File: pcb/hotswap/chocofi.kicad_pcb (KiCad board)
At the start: 2 copper layers, 111.3 x 90 mm, 61 parts, among them J2 Conn_01x05, J3 Conn_01x02_Female, SW1 SW_SPDT, SW10 SW_PUSH, SW11 SW_PUSH, SW12 SW_PUSH, SW14 SW_PUSH, SW15 SW_PUSH, SW16 SW_PUSH, SW17 SW_PUSH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

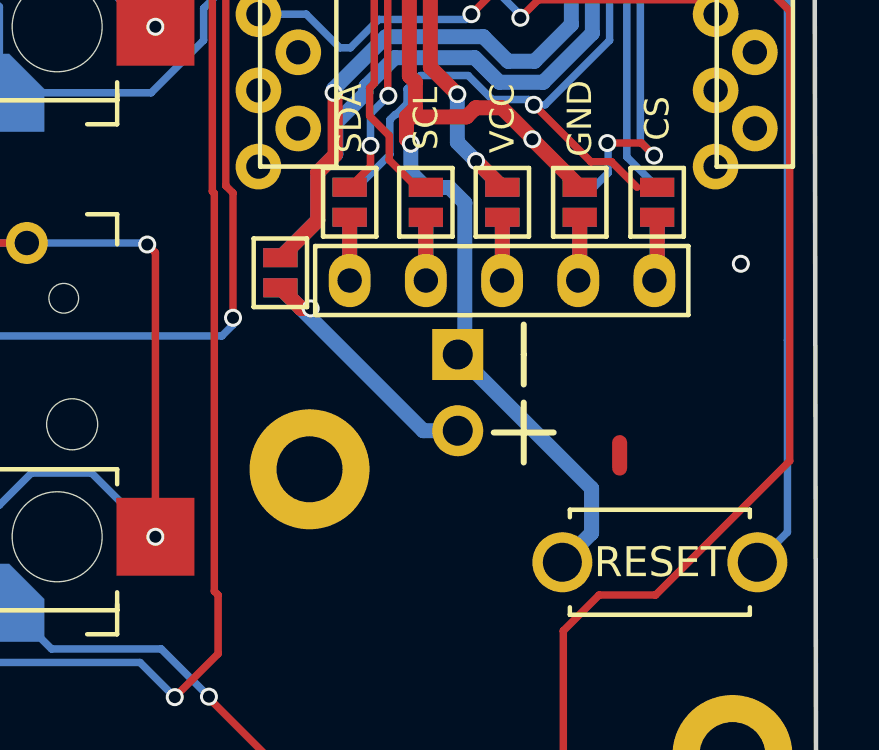
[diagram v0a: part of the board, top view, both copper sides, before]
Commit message: move reset button
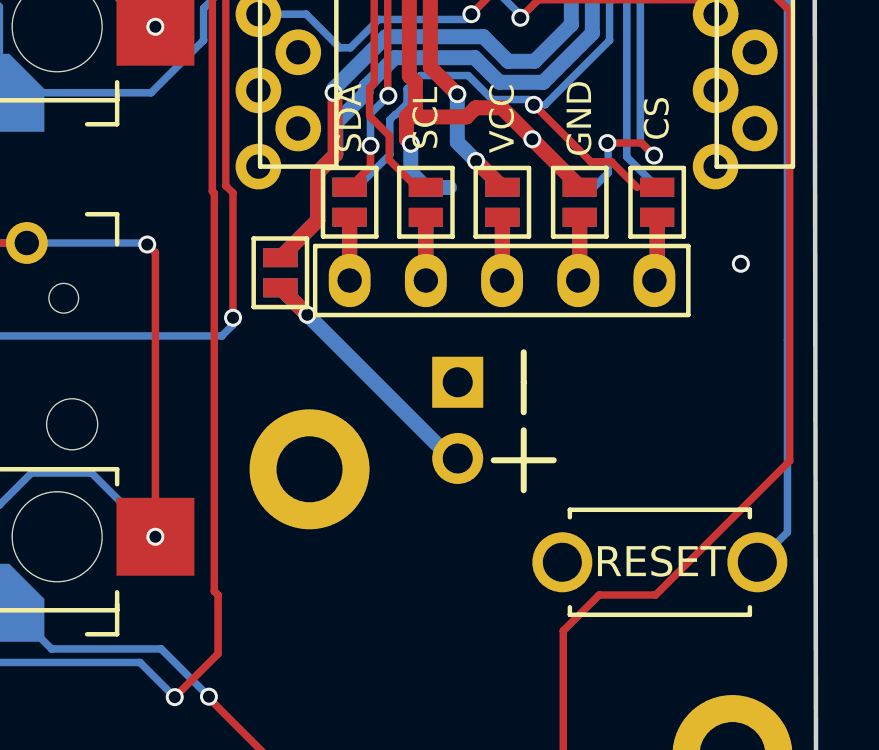
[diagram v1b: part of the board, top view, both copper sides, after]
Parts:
- moved J3 0.92 mm to (176.3, 94.0)
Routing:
- net GND: track 79.1 -> 63.2 mm
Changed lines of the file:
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@@
 		)
 		(pad_to_mask_clearance 0.2)
-		(solder_mask_min_width 0.1)
 		(allow_soldermask_bridges_in_footprints no)
 		(aux_axis_origin 145.73 12.66)
@@
 		(fp_arc
 			(start -1 3.7)
-			(mid -2.060661 3.260661)
+			(mid -2.060662 3.260662)
 			(end -2.5 2.2)
 			(stroke
@@
 		(fp_arc
 			(start -1 3.7)
-			(mid -2.060661 3.260661)
+			(mid -2.060662 3.260662)
 			(end -2.5 2.2)
 			(stroke
@@
 		)
 		(fp_line
-			(start 7 4.999999)
+			(start 7 4.999998)
 			(end 9.5 5)
 			(stroke
@@
 	(footprint "kbd:Battery_TH"
 		(layer "F.Cu")
-		(at 176.2625 93.075)
+		(at 176.2625 94)
 		(descr "Through hole straight pin header, 1x02, 2.54mm pitch, single row")
 		(tags "Through hole pin header THT 1x02 2.54mm single row")
 		(property "Reference" "J3"
-			(at 0 -2.33 360)
+			(at 0 -2.33 0)
 			(layer "Dwgs.User")
 			(effects
@@
 		)
 		(property "Value" "Conn_01x02_Female"
-			(at 0 4.87 360)
+			(at 0 4.87 0)
 			(layer "F.Fab")
 			(effects
@@
 		)
 		(property "Footprint" ""
-			(at 0 0 360)
+			(at 0 0 0)
 			(layer "F.Fab")
 			(hide yes)
@@
 		)
 		(property "Datasheet" ""
-			(at 0 0 360)
+			(at 0 0 0)
 			(layer "F.Fab")
 			(hide yes)
@@
 		)
 		(property "Description" "Generic connector, single row, 01x02, script generated (kicad-library-utils/schlib/autogen/connector/)"
-			(at 0 0 360)
+			(at 0 0 0)
 			(layer "F.Fab")
 			(hide yes)
@@
 	)
 	(segment
-		(start 181.66 96.861)
-		(end 181.66 96.01)
-		(width 0.5)
-		(layer "F.Cu")
-		(net 21)
-	)
-	(segment
 		(start 178.75 85.86802)
 		(end 178.75 85.9)
@@
 	)
 	(segment
-		(start 175.98824 87.50762)
-		(end 176.5 88.01938)
-		(width 0.5)
-		(layer "B.Cu")
-		(net 21)
-	)
-	(segment
-		(start 176.5 92.8375)
-		(end 176.2625 93.075)
-		(width 0.5)
-		(layer "B.Cu")
-		(net 21)
-	)
-	(segment
 		(start 174.7 86.05)
 		(end 174.7 87.00762)
@@
 	)
 	(segment
-		(start 180.725 99.025)
-		(end 180.725 97.5375)
-		(width 0.5)
-		(layer "B.Cu")
-		(net 21)
-	)
-	(segment
-		(start 179.75 100)
-		(end 180.725 99.025)
-		(width 0.5)
-		(layer "B.Cu")
-		(net 21)
-	)
-	(segment
-		(start 176.5 88.01938)
-		(end 176.5 92.8375)
-		(width 0.5)
-		(layer "B.Cu")
-		(net 21)
-	)
-	(segment
-		(start 180.725 97.5375)
-		(end 176.2625 93.075)
-		(width 0.5)
-		(layer "B.Cu")
-		(net 21)
-	)
-	(segment
 		(start 182.4404 66.4904)
 		(end 184.86 66.4904)
@@
 	)
 	(segment
-		(start 171.361564 91.538436)
-		(end 171.037676 91.538436)
+		(start 170.35038 90.85076)
+		(end 171.24981 91.75019)
 		(width 0.5)
 		(layer "F.Cu")
@@
 	)
 	(segment
-		(start 171.037676 91.538436)
-		(end 170.35 90.85076)
+		(start 170.35 90.85076)
+		(end 170.35038 90.85076)
 		(width 0.5)
 		(layer "F.Cu")
@@
 	)
 	(via
-		(at 171.361564 91.538436)
+		(at 171.24981 91.75019)
 		(size 0.6)
 		(drill 0.4)
@@
 	)
 	(segment
-		(start 175.11462 95.615)
+		(start 176.2625 96.54)
+		(end 176.03962 96.54)
+		(width 0.5)
+		(layer "B.Cu")
+		(net 44)
+	)
+	(segment
+		(start 171.24981 91.75019)
 		(end 170.35 90.85038)
 		(width 0.5)
@@
 	)
 	(segment
-		(start 176.2625 95.615)
-		(end 175.11462 95.615)
+		(start 176.03962 96.54)
+		(end 171.24981 91.75019)
 		(width 0.5)
 		(layer "B.Cu")
